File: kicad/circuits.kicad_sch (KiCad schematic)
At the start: 39 parts

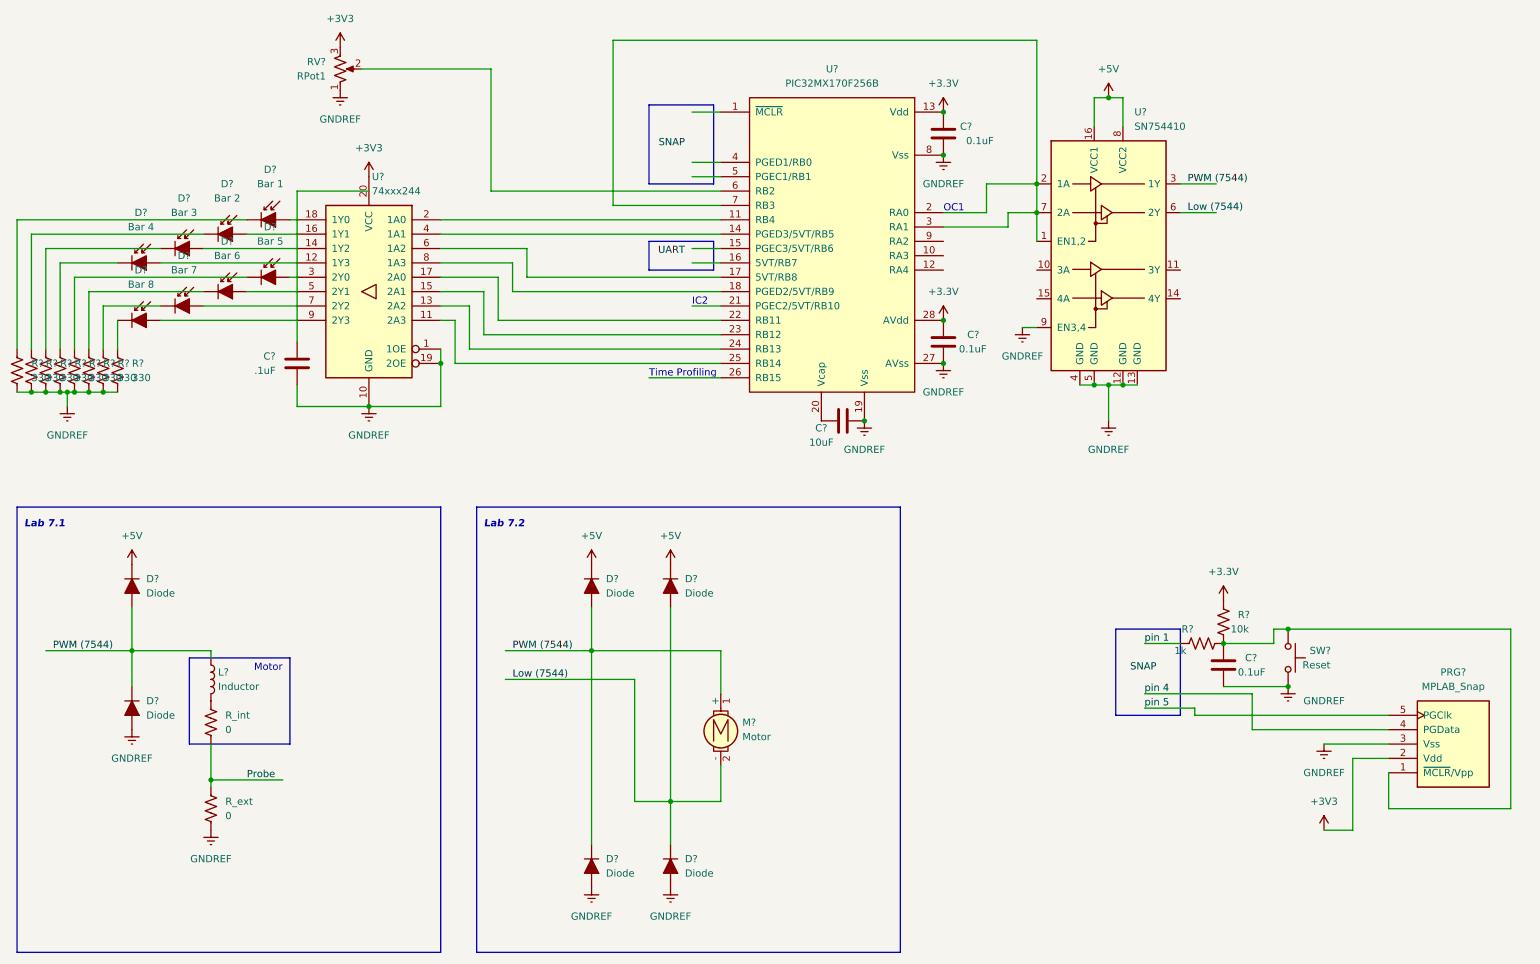
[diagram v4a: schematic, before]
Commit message: [stable] Set period < electrical time constant
* Motor rise time without external resistance: 198us
* Set period to 25us
* Mapped dc to rpm
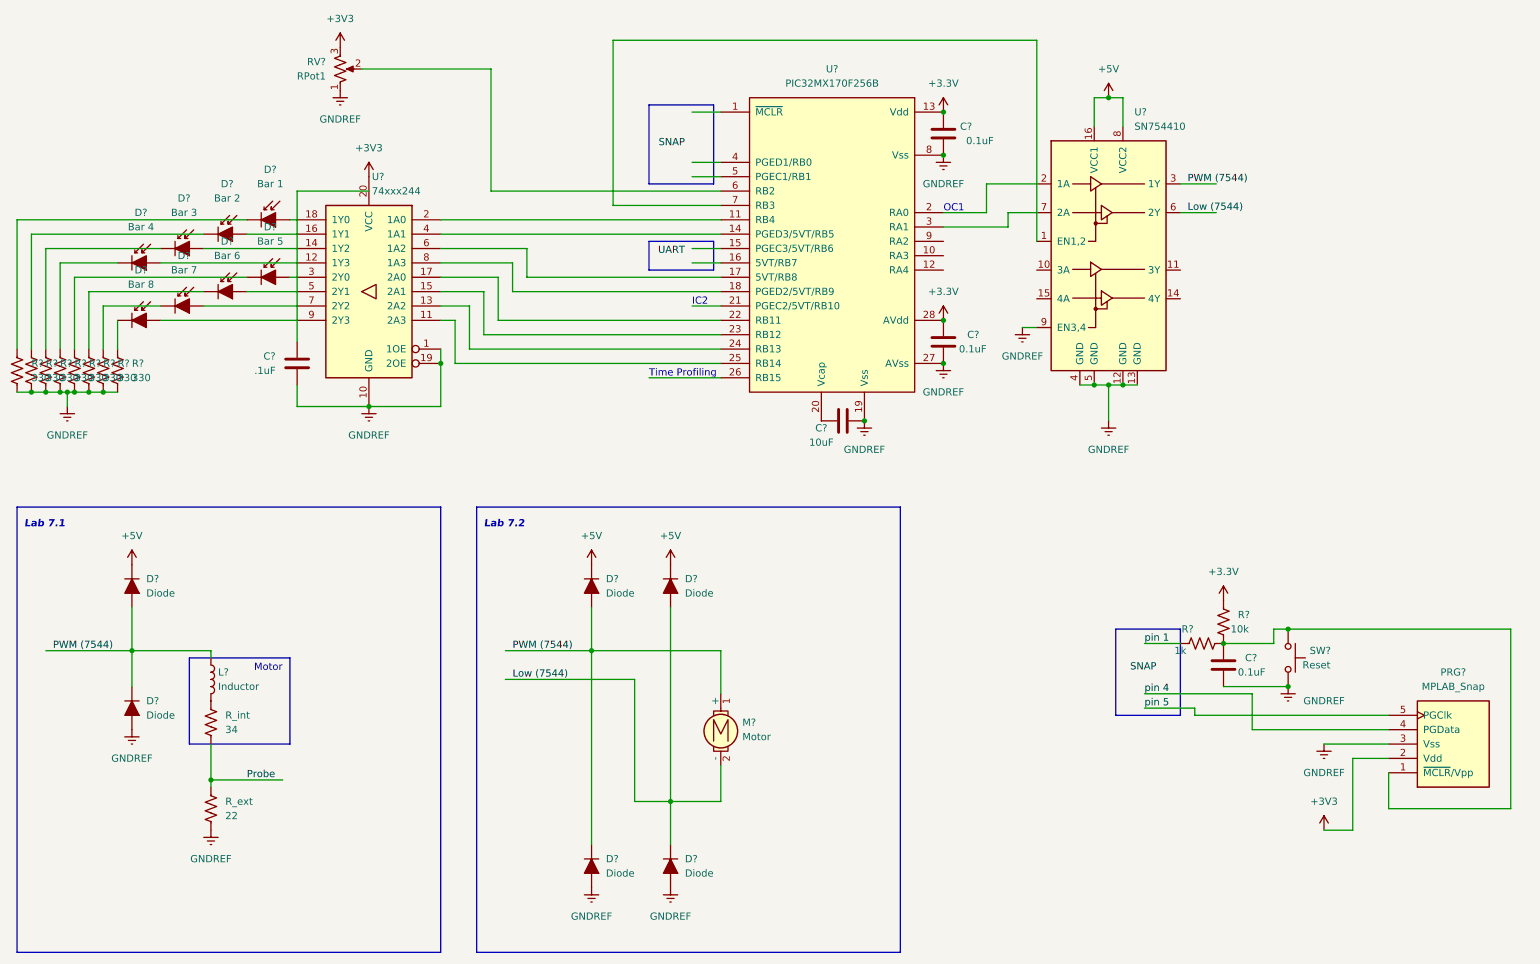
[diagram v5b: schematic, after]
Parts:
- R_ext: value 0 -> 22
- R_int: value 0 -> 34
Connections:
- new net: U?.2 (1A), U?.2 (RA0)
- new net: U?.3 (RA1), U?.7 (2A)
- new net: U?.1 (EN1,2), U?.7 (RB3)
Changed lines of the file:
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@@
   (junction (at 31.75 83.82) (diameter 0) (color 0 0 0 0)
   )
-  (junction (at 196.85 52.07) (diameter 0) (color 0 0 0 0)
-  )
   (junction (at 180.34 34.29) (diameter 0) (color 0 0 0 0)
   )
   (junction (at 78.74 86.36) (diameter 0) (color 0 0 0 0)
   )
-  (junction (at 196.85 46.99) (diameter 0) (color 0 0 0 0)
-  )
   (junction (at 166.37 88.9) (diameter 0) (color 0 0 0 0)
   )
@@
     (stroke (width 0) (type default) (color 0 0 0 0))
   )
-  (wire (pts (xy 196.85 46.99) (xy 196.85 52.07))
+  (wire (pts (xy 196.85 21.59) (xy 196.85 57.15))
     (stroke (width 0) (type default) (color 0 0 0 0))
   )
@@
     (stroke (width 0) (type default) (color 0 0 0 0))
   )
-  (wire (pts (xy 196.85 21.59) (xy 196.85 46.99))
-    (stroke (width 0) (type default) (color 0 0 0 0))
-  )
   (wire (pts (xy 121.92 50.8) (xy 121.92 21.59))
     (stroke (width 0) (type default) (color 0 0 0 0))
@@
   )
   (wire (pts (xy 50.8 130.81) (xy 50.8 129.54))
-    (stroke (width 0) (type default) (color 0 0 0 0))
-  )
-  (wire (pts (xy 196.85 52.07) (xy 196.85 57.15))
     (stroke (width 0) (type default) (color 0 0 0 0))
   )
@@
       (effects (font (size 1.27 1.27)) (justify left))
     )
-    (property "Value" "0" (id 1) (at 53.34 143.5099 0)
+    (property "Value" "34" (id 1) (at 53.34 143.5099 0)
       (effects (font (size 1.27 1.27)) (justify left))
     )
@@
       (effects (font (size 1.27 1.27)) (justify left))
     )
-    (property "Value" "0" (id 1) (at 53.34 158.7499 0)
+    (property "Value" "22" (id 1) (at 53.34 158.7499 0)
       (effects (font (size 1.27 1.27)) (justify left))
     )
@@
     )
     (path "/7f857093-bed4-484c-9d6c-b23384063141"
-      (reference "R_ext") (unit 1) (value "0") (footprint "")
+      (reference "R_ext") (unit 1) (value "22") (footprint "")
     )
     (path "/04c9935a-b8c7-4494-b100-23869fd32068"
-      (reference "R_int") (unit 1) (value "0") (footprint "")
+      (reference "R_int") (unit 1) (value "34") (footprint "")
     )
     (path "/eb0d2ab4-d10d-41f8-be7c-0e5badacc448"
